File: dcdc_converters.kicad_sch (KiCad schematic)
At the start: 18 parts, among them U5 AP62301WU-7, U6 AP62301WU-7

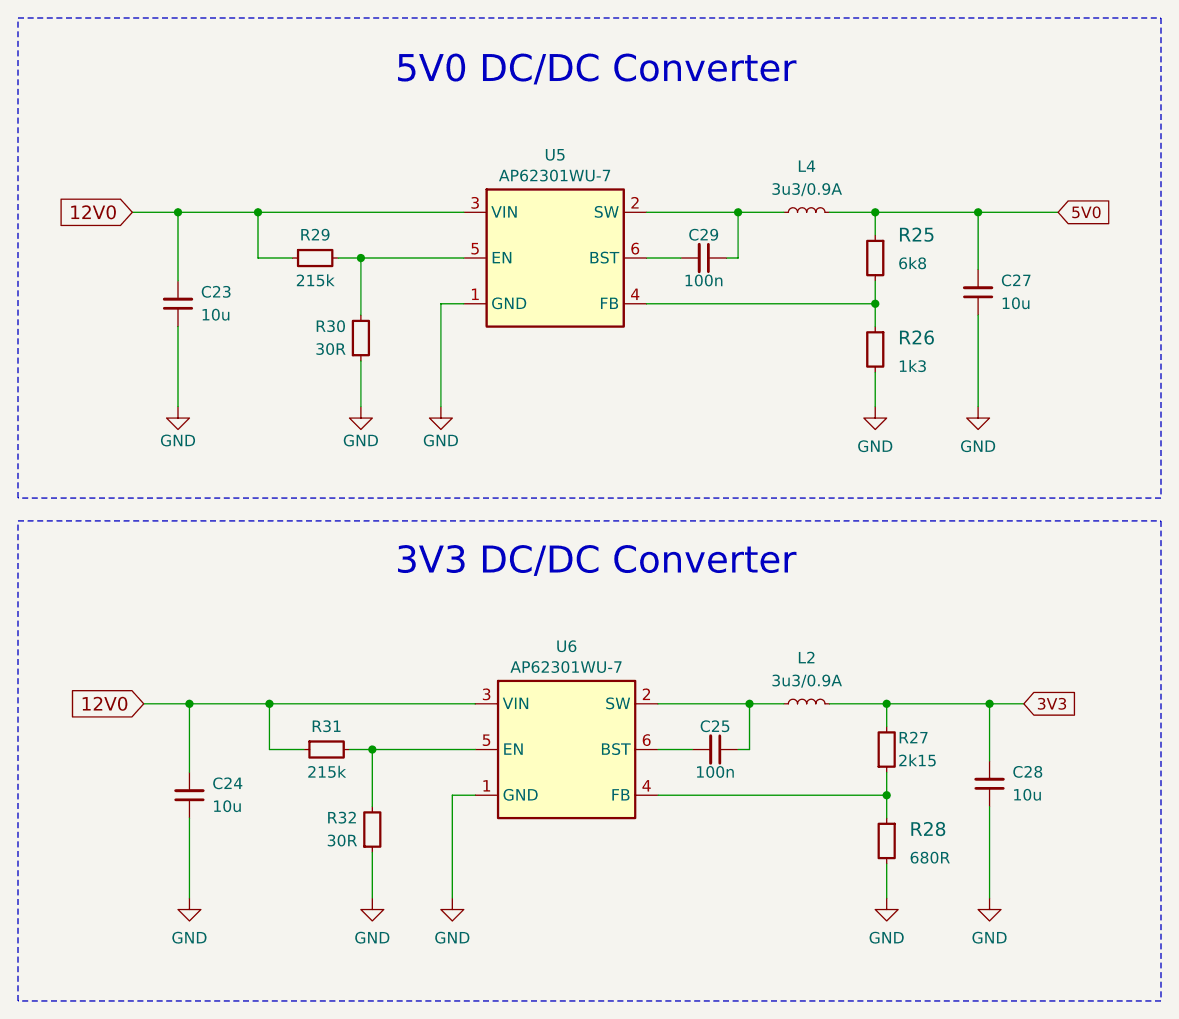
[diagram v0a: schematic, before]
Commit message: [#57006] Change C17, R25, R26
Improve connections
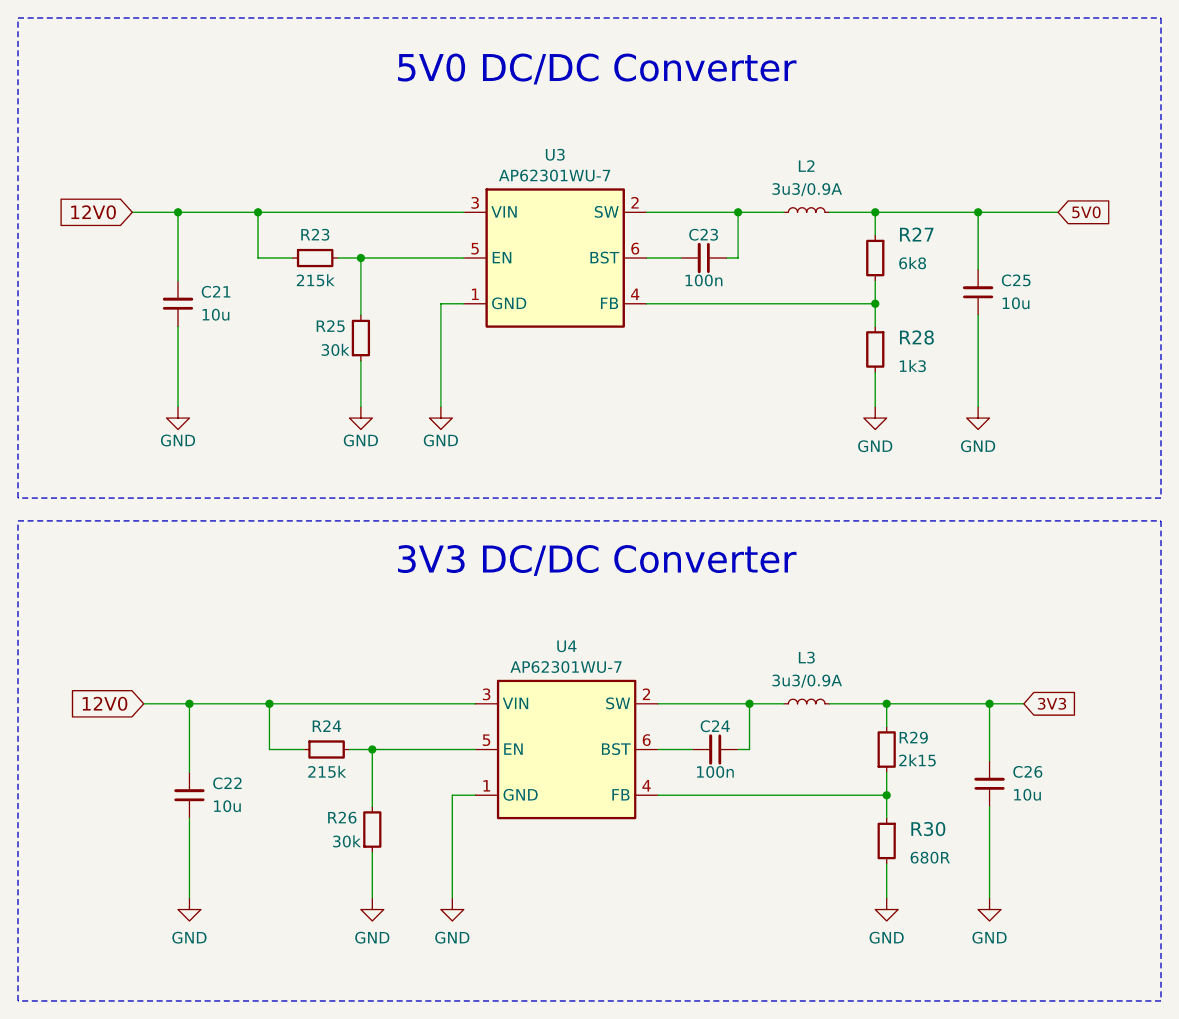
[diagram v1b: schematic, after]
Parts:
- R25: renamed from R30; symbol antmicroResistors0402:R_30R_0402 -> antmicroResistors0402:R_30k_0402; MPN CR0402-FX-30R0GLF -> CR0402-FX-3002GLF; Val 30R -> 30k
- R26: renamed from R32; symbol antmicroResistors0402:R_30R_0402 -> antmicroResistors0402:R_30k_0402; MPN CR0402-FX-30R0GLF -> CR0402-FX-3002GLF; Val 30R -> 30k
- renumbered C23 to C21, C24 to C22, C29 to C23, C25 to C24, C27 to C25, C28 to C26, L4 to L2, L2 to L3, R29 to R23, R31 to R24, R25 to R27, R26 to R28, R27 to R29, R28 to R30, U5 to U3, U6 to U4
